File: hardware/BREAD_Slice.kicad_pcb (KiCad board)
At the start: 2 copper layers, 70 x 100 mm, 60 parts, among them J1 Conn_01x10_Female

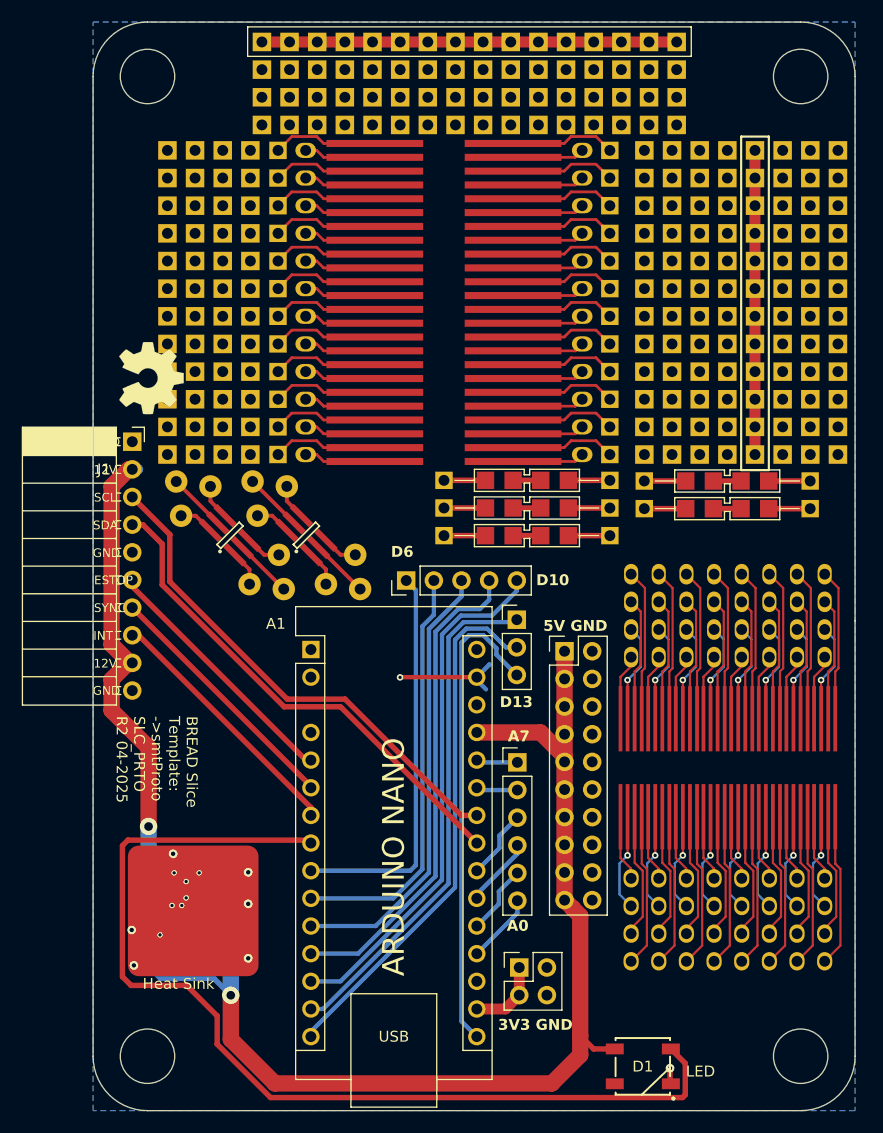
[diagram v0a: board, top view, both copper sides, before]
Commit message: tweak to add more ground pins, need to relocate protolib
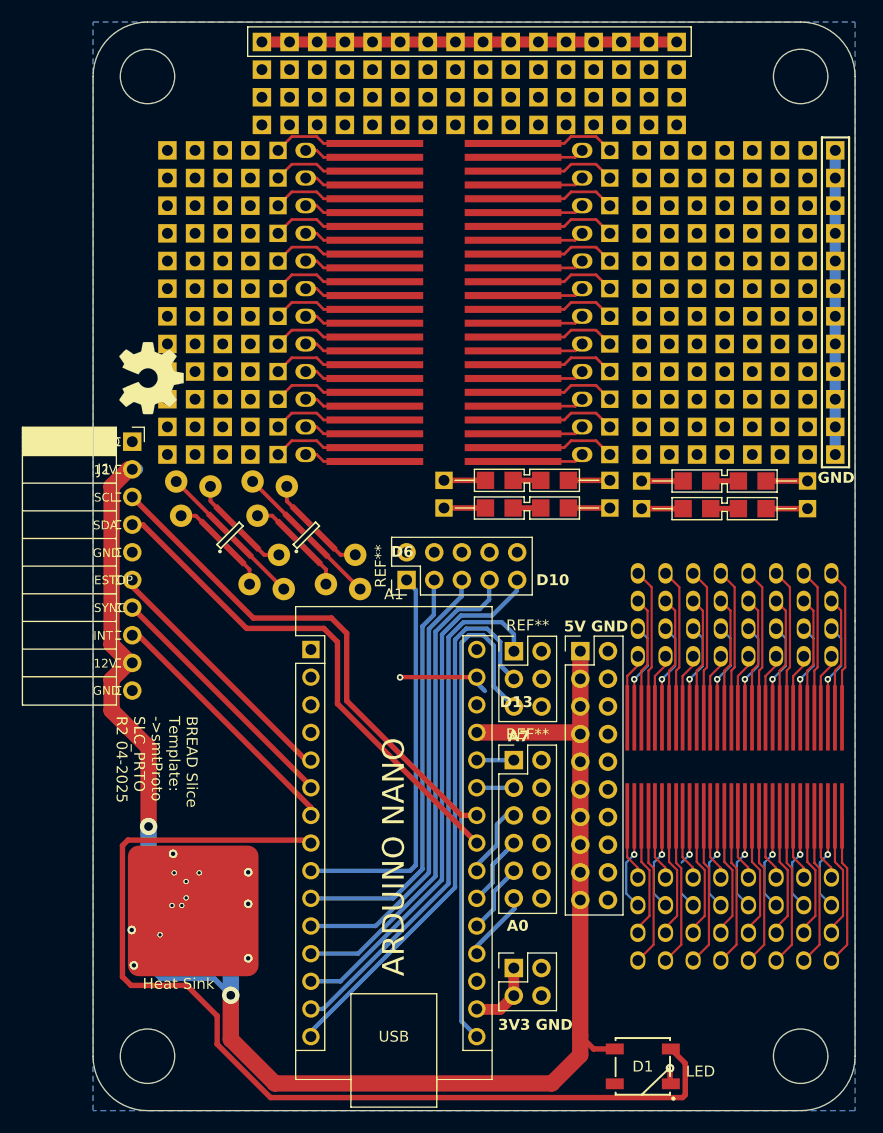
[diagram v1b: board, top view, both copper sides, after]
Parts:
- removed the ? at (162.5, 87.0)
- removed the REF** at (161.5, 94.7)
- removed the REF** at (161.6, 107.8)
- removed the REF** at (151.4, 91.1)
- added REF**: PinHeader_2x03_P2.54mm_Vertical, Connector_PinHeader_2.54mm:PinHeader_2x03_P2.54mm_Vertical, F.Cu at (161.3, 97.6)
- added REF**: PinHeader_2x05_P2.54mm_Vertical, Connector_PinHeader_2.54mm:PinHeader_2x05_P2.54mm_Vertical, F.Cu at (151.4, 91.0)
- added REF**: PinHeader_2x06_P2.54mm_Vertical, Connector_PinHeader_2.54mm:PinHeader_2x06_P2.54mm_Vertical, F.Cu at (161.2, 107.6)
- A1: footprint Module:Arduino_Nano -> KMLib_Boards_Modules:Arduino_Nano_Headers
- moved REF** 1.45 mm to (167.4, 97.6)
- moved ? 0.62 mm to (177.7, 108.2)
- moved ? 0.62 mm to (182.8, 108.2)
- moved ? 0.62 mm to (172.6, 108.2)
- moved ? 0.62 mm to (185.3, 108.2)
- moved ? 0.62 mm to (190.4, 108.2)
- moved ? 0.62 mm to (175.2, 108.2)
- moved ? 0.62 mm to (187.9, 108.2)
- moved ? 0.62 mm to (180.3, 108.2)
- moved REF** 0.50 mm to (161.2, 126.7)
- moved ? 0.25 mm to (183.2, 59.2)
- moved ? 0.25 mm to (183.2, 69.4)
- moved ? 0.25 mm to (183.2, 79.5)
- moved ? 0.25 mm to (173.0, 69.4)
- moved ? 0.25 mm to (173.0, 79.5)
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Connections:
- ? pad 10: (no net) -> GND (x3)
- ? pad 11: (no net) -> GND (x3)
- ? pad 12: (no net) -> GND (x3)
- ? pad 13: (no net) -> GND (x3)
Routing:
- net (no net): track 1002.1 -> 964.0 mm
- net GND: track 222.6 -> 246.4 mm
- net /D13: track 44.0 -> 46.8 mm
- net /D12: track 48.7 -> 50.9 mm
- net /D11: track 47.0 -> 48.7 mm
- net /I2C_DAT: track 46.0 -> 47.1 mm
- net /I2C_CLK: track 46.3 -> 47.4 mm
- net /A3: track 6.41 -> 6.97 mm

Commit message: reattach all footprints and revise layout
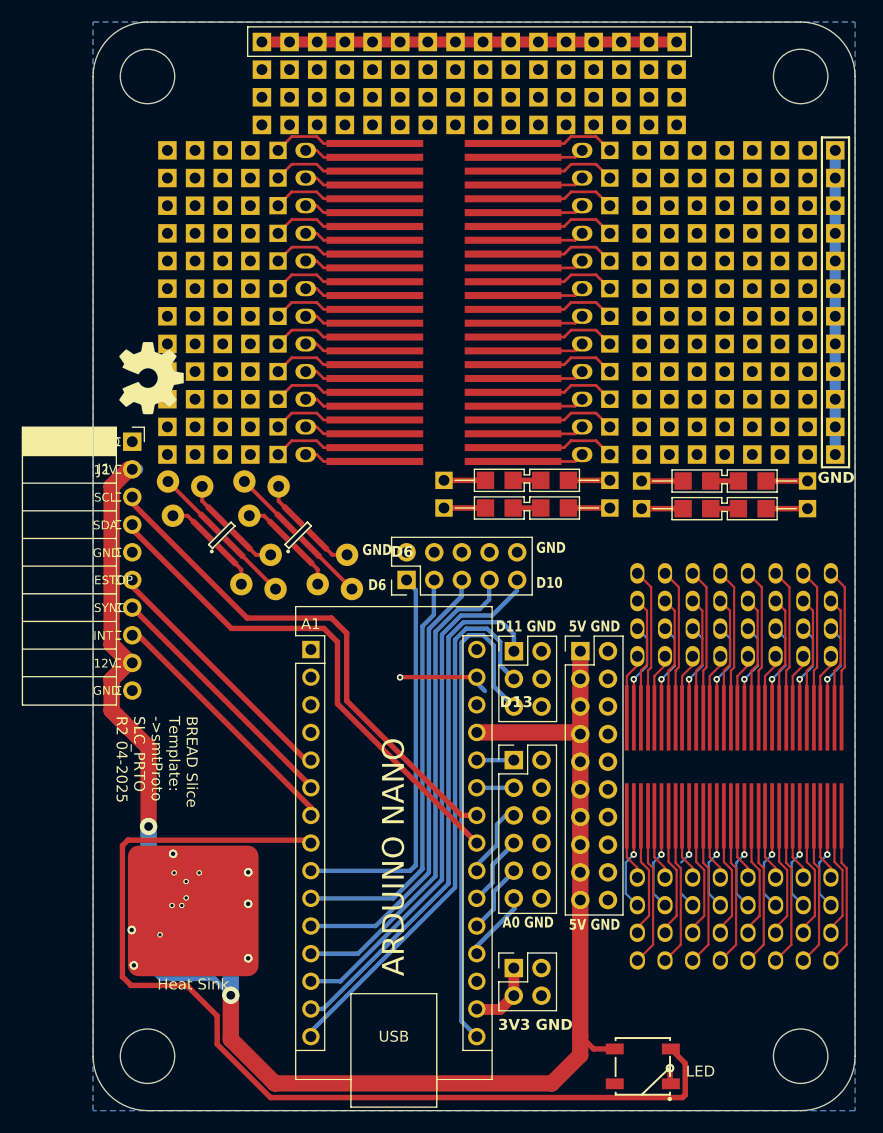
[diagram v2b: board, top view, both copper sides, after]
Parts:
- ? (x12): footprint PROTO-SOIC-50 -> KMLib_Proto:SOIC_1.27mm_TH_AnnularPad
- ? (x8): footprint kicad_wrk:PROTO-SSOP-0.65 -> KMLib_Proto:SSOP_0.65mm_TH_AnnularPad
- ? (x13): footprint kicad_wrk:PROTO-GRID4X4-100-SQUARE -> KMLib_Proto:Grid_TH_SquarePad_4x4_2.54mm
- ? (x2): footprint kicad_wrk:PROTO-SOT-23-6 -> KMLib_Proto:SOT-23-6_TH_AnnularPad
- ? (x4): footprint kicad_wrk:PROTO-LED -> KMLib_Proto:1206_HandSolder_Dual_TH_AnnularPad
- D1: footprint SparkFun-LED:WS2812-5050-4PIN -> KMLib_IC_SMD:WS2812-5050-4PIN
- HS1: footprint KML-Custom:Thermal Pad -> KMLib_Mounting:Thermal Pad
- moved ? 0.75 mm to (134.4, 86.9)
- moved ? 0.75 mm to (141.4, 86.9)
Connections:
- A1 pad 3: (no net) -> unconnected-(A1-~{RESET}-Pad3)
- REF** pad 2: (no net) -> GND (x3)
- REF** pad 4: (no net) -> GND (x3)
- REF** pad 6: (no net) -> GND (x3)
- REF** pad 10: (no net) -> GND (x2)
- REF** pad 8: (no net) -> GND (x2)
- REF** pad 12: (no net) -> GND
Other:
- board text added: "A0 GND"
- board text added: "D11 GND"
- board text added: "GND D10"
- board text added: "GND D6"
- board text removed: "A0"
- board text removed: "A7"
- board text removed: "D10"
